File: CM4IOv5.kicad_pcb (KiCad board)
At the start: 4 copper layers, 85.1 x 55.9 mm, 120 parts, among them J1 Conn_01x02, J10 HDMI_C_1.4, J11 HDMI_C_1.4, J12 Conn_02x07_Odd_Even, J13 Conn_01x03, J14 Conn_01x03, J15 Audio OUT, J16 Micro_SD_Card_Det, J2 Bus_M.2_Socket_B, J3 USB_OTG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

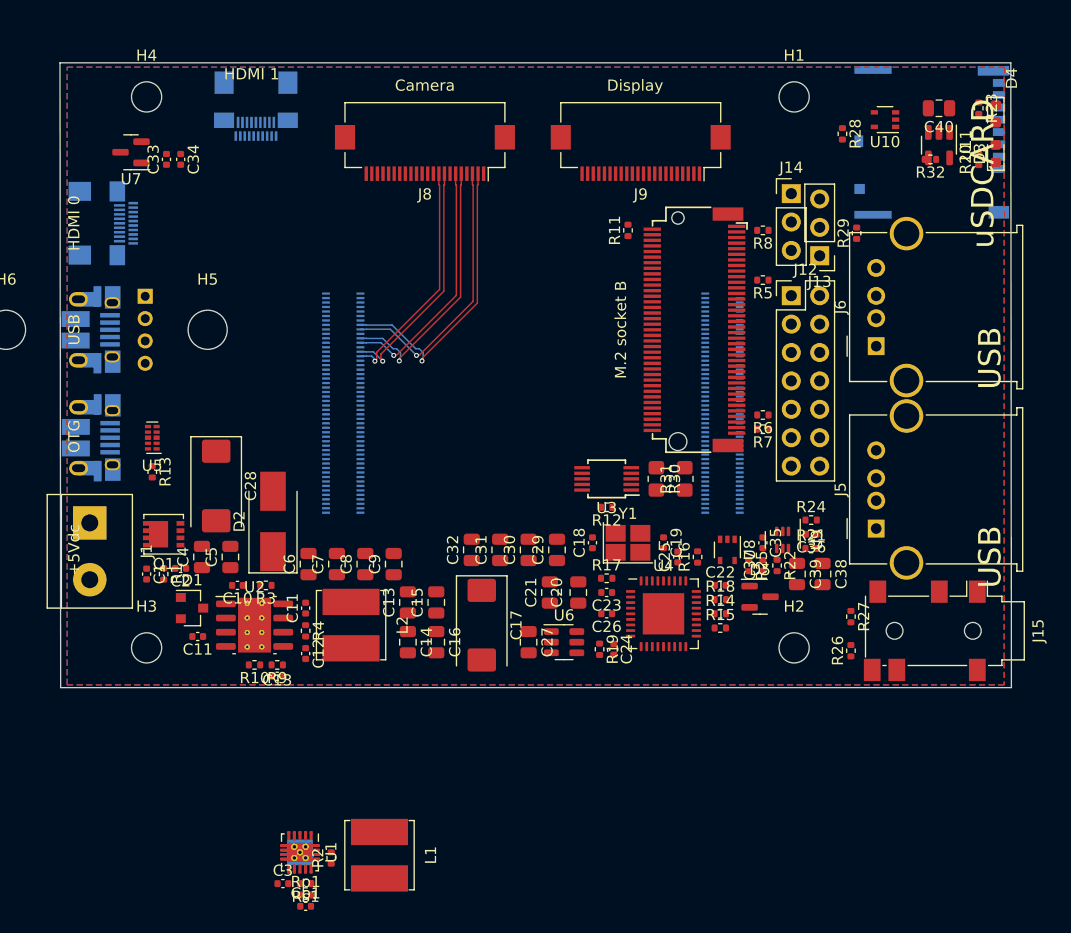
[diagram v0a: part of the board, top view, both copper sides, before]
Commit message: Initial routing of high speed signals
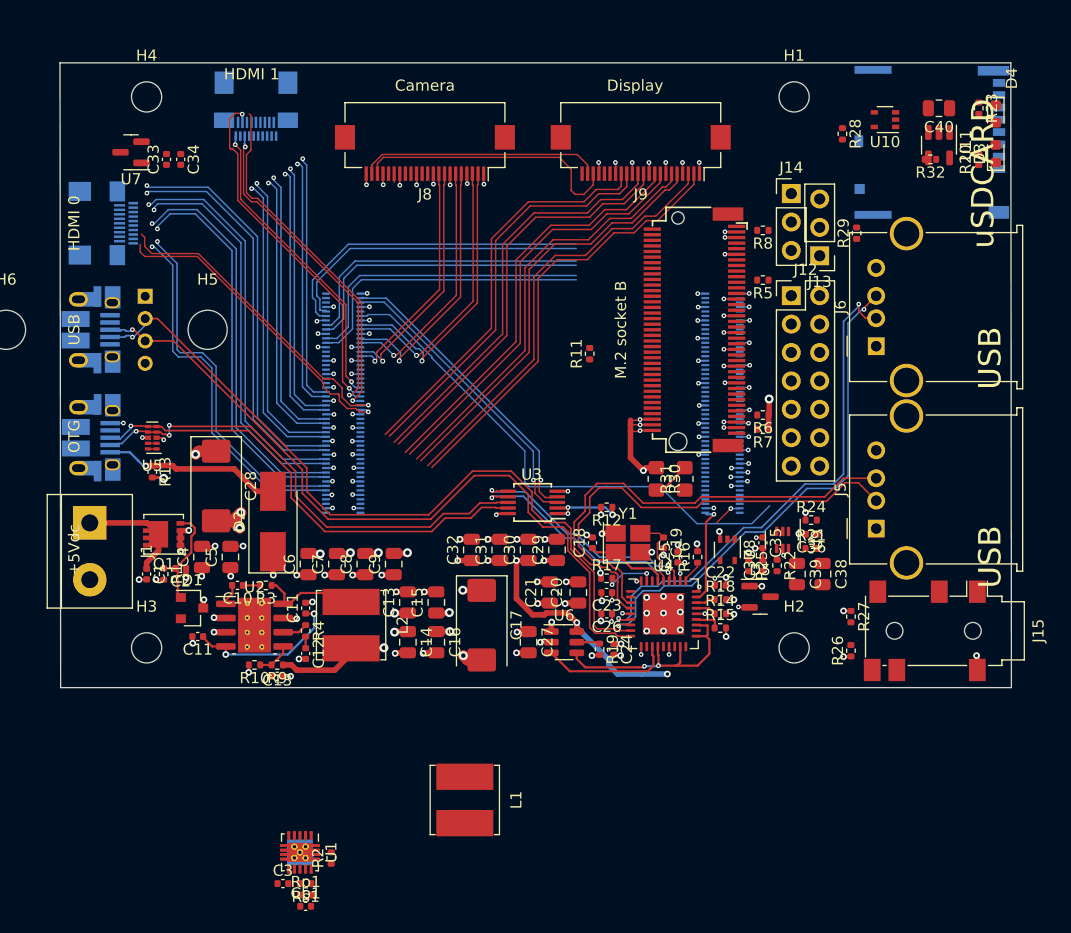
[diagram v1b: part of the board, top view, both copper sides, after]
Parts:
- moved R11 11.5 mm to (164.2, 105.0)
- moved L1 9.09 mm to (153.0, 144.9)
- moved U3 6.95 mm to (159.1, 118.3)
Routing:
- net GND: track 530.4 -> 119.2 mm, vias 0 -> 143
- net /+3.3v: track 0.00 -> 148.0 mm, vias 0 -> 27
- net /USB2-HUB/VBUS: track 0.00 -> 115.3 mm, vias 0 -> 7
- net /+5v: track 4.09 -> 116.8 mm, vias 0 -> 21
- net /USB2-HUB/HD4_N: track 0.00 -> 69.4 mm, vias 0 -> 1
- net /USB2-HUB/HD4_P: track 0.00 -> 68.3 mm, vias 0 -> 1
- net /+3.3vSSD: track 0.00 -> 68.1 mm, vias 0 -> 7
- net /CM4_GPIO (GPIO, SDCARD)/TV_OUT: track 0.00 -> 46.8 mm
- net /USB2-HUB/HD3_N: track 0.00 -> 45.9 mm, vias 0 -> 2
- net /USB2-HUB/HD3_P: track 0.00 -> 45.5 mm, vias 0 -> 2
- net /USB2-HUB/USBD_N: track 0.00 -> 43.1 mm, vias 0 -> 3
- net /USB2-HUB/USBD_P: track 0.00 -> 42.3 mm, vias 0 -> 1
- net /USB2-HUB/HD2_P: track 0.00 -> 41.8 mm
- net /USB2-HUB/HD2_N: track 0.00 -> 41.3 mm
- net /CM4_HighSpeed/DSI1_D0_N: track 0.00 -> 39.2 mm
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- removed copper zone on In2.Cu, net /+3.3v
- removed copper zone on B.Cu, net GND
- removed copper zone on F.Cu, net GND
- removed copper zone on In2.Cu, net GND

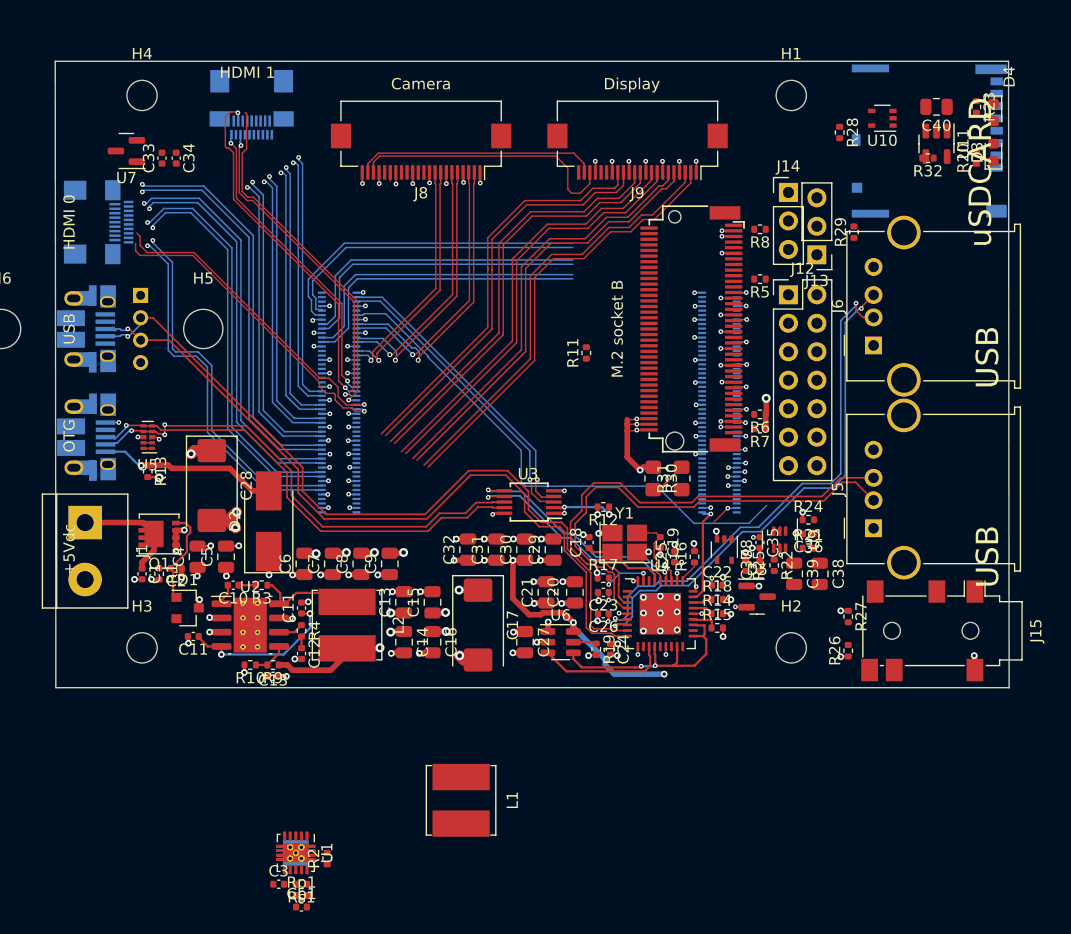
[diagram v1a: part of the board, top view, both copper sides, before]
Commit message: Aditional routing
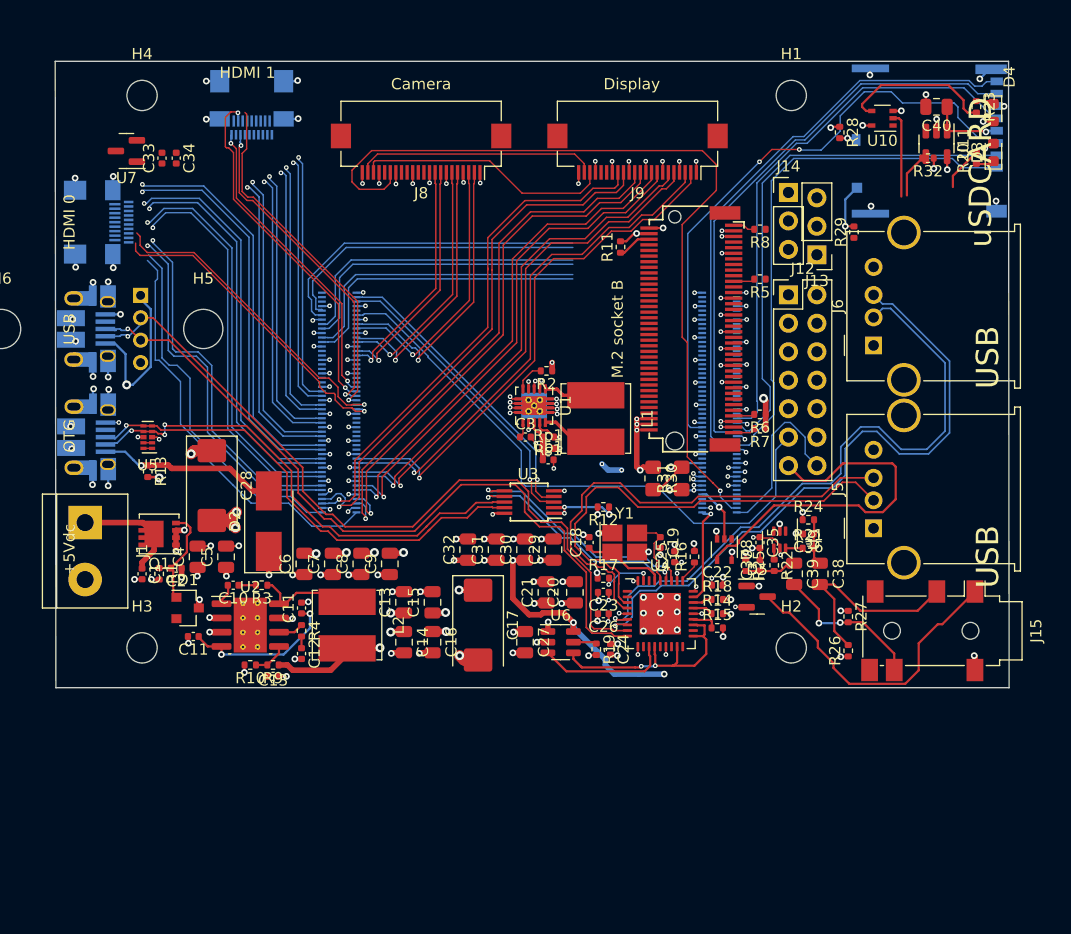
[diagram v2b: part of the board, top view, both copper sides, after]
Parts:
- moved R2 47.7 mm to (160.7, 106.6), turned to 180 degrees
- moved Cp1 45.6 mm to (160.8, 114.5)
- moved Rp1 45.6 mm to (160.8, 113.5)
- moved Rs1 45.6 mm to (160.8, 112.5)
- moved C3 45.6 mm to (158.8, 112.5)
- moved U1 45.2 mm to (159.6, 109.7)
- moved L1 36.1 mm to (165.1, 110.8)
- moved R11 9.93 mm to (167.2, 95.5)
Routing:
- net /+3.3v: track 148.0 -> 254.6 mm, vias 27 -> 37
- net /+5v: track 116.8 -> 188.3 mm, vias 21 -> 26
- net /CM4_HighSpeed/CAM_GPIO: track 3.36 -> 73.9 mm
- net /CM4_GPIO (GPIO, SDCARD)/SD_CMD: track 0.00 -> 54.5 mm, vias 0 -> 2
- net /CM4_GPIO (GPIO, SDCARD)/SD_DAT1: track 0.00 -> 53.0 mm
- net /CM4_GPIO (GPIO, SDCARD)/SD_DAT0: track 0.00 -> 51.4 mm
- net /CM4_GPIO (GPIO, SDCARD)/SD_CLK: track 0.00 -> 48.6 mm
- net /CM4_GPIO (GPIO, SDCARD)/SD_DAT2: track 0.00 -> 47.0 mm
- net /CM4_GPIO (GPIO, SDCARD)/SD_DAT3: track 0.00 -> 46.4 mm
- net GND: track 119.2 -> 160.0 mm, vias 143 -> 186
- net /CM4_HighSpeed/HDMI0_SDA: track 0.00 -> 36.8 mm
- net Net-(J12-Pad13): track 0.00 -> 32.8 mm
- net /CM4_HighSpeed/HDMI0_SCL: track 0.00 -> 32.4 mm
- net Net-(D5-Pad3): track 0.00 -> 27.1 mm
- net /USB2-HUB/VBUS: track 115.3 -> 140.3 mm, vias 7 -> 8
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
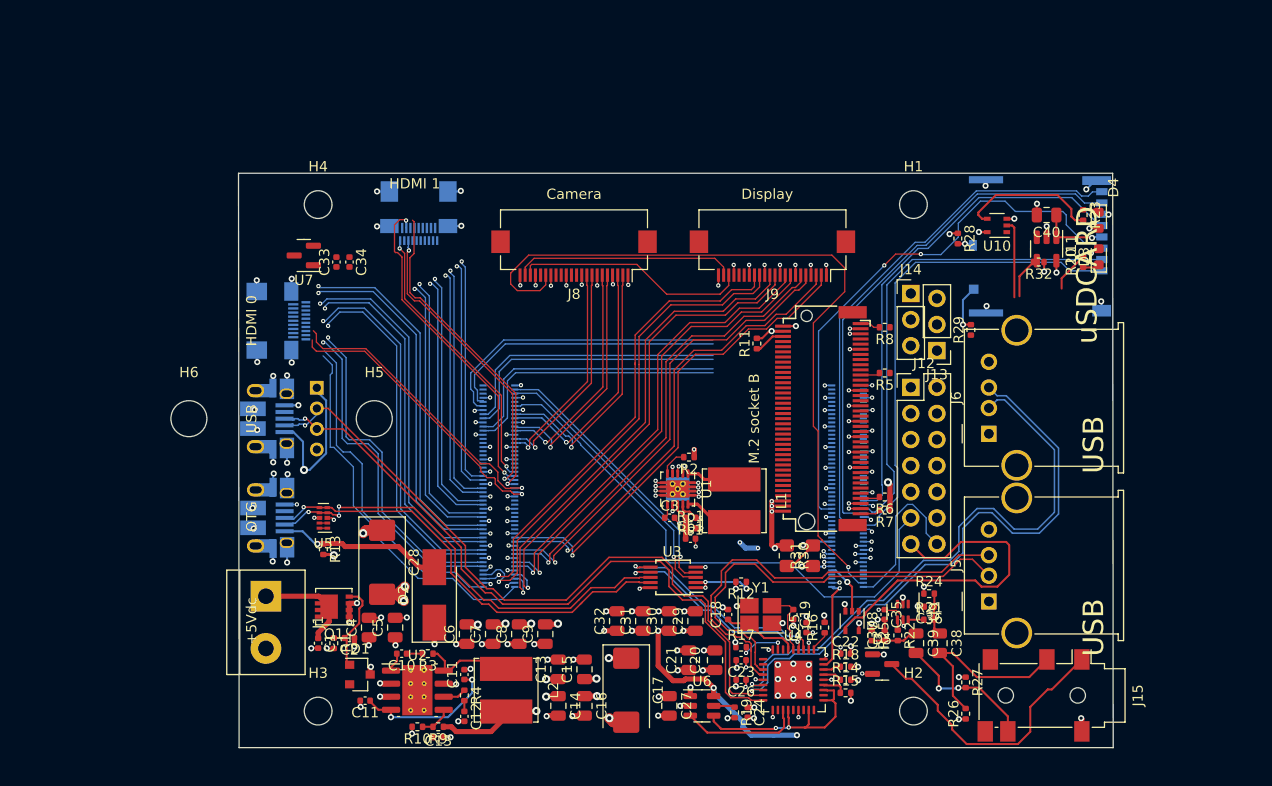
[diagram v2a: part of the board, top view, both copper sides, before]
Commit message: Adding normal size HDMI connectors
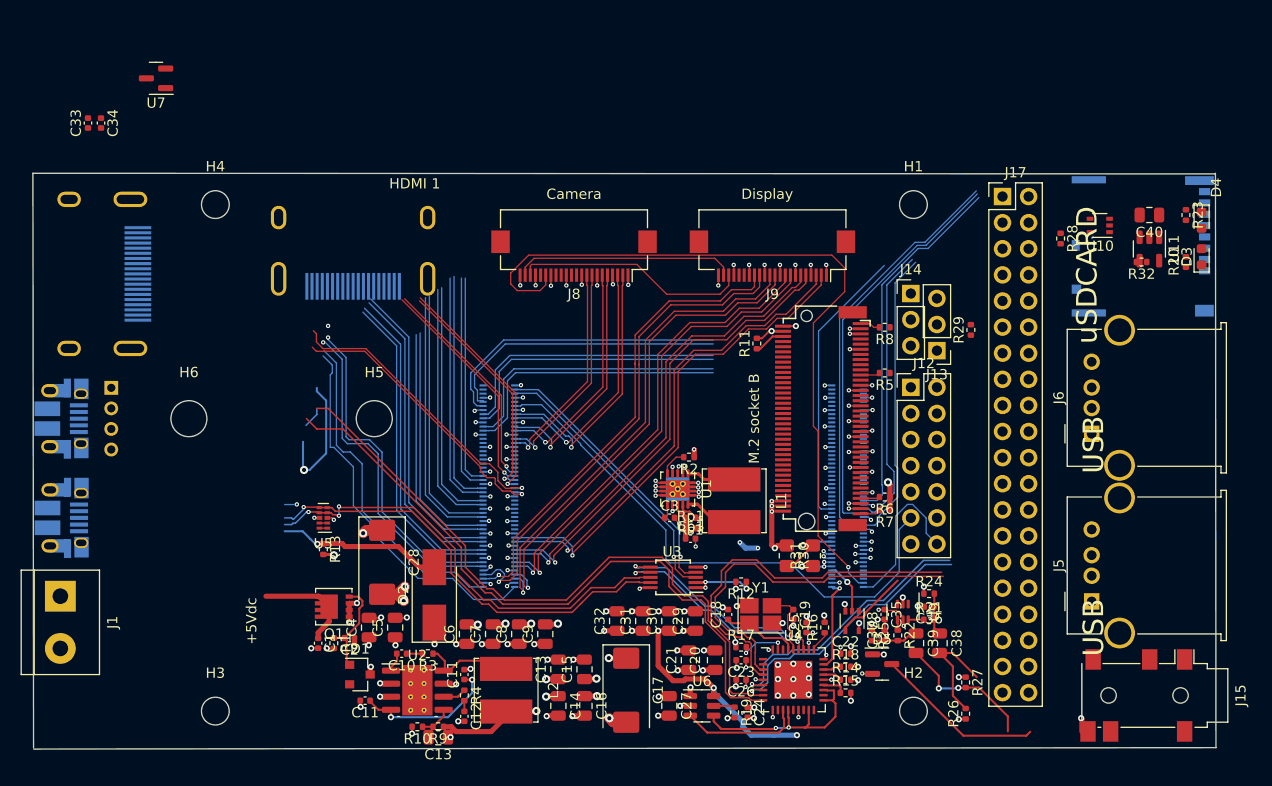
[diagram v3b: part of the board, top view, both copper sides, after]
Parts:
- added J17: THD-20-R, Connector_PinHeader_2.54mm:PinHeader_2x20_P2.54mm_Vertical, F.Cu at (191.2, 81.2)
- C11: value nf -> 100n
- C13: value nf -> 10u; footprint Capacitor_SMD:C_0402_1005Metric -> Capacitor_SMD:C_0805_2012Metric
- J10, J11: footprint Connector_HDMI:HDMI_Micro-D_Molex_46765-0x01 -> CM4IO:EDAC 690-019-298-412
- moved C34 27.7 mm to (103.5, 74.1)
- moved C33 27.7 mm to (102.2, 74.1)
- moved U7 22.4 mm to (108.8, 69.8)
- moved J1 20.0 mm to (99.5, 120.1)
- moved J3 20.0 mm to (98.5, 112.5)
- moved J4 20.0 mm to (104.4, 99.9)
- moved J7 20.0 mm to (98.5, 102.9)
- moved J10 13.1 mm to (106.3, 88.8)
- moved J11 10.6 mm to (128.0, 89.3)
- moved C40 10.0 mm to (205.4, 83.0)
- moved D3 10.0 mm to (210.5, 87.1)
- moved D4 10.0 mm to (210.5, 83.6)
- moved H3 10.0 mm to (114.6, 131.3)
- moved H4 10.0 mm to (114.6, 82.0)
- moved J15 10.0 mm to (204.2, 129.8)
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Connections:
- C13 pad 1: /+3.3v -> /+3.3vSSD
- C13 pad 2: Net-(C13-Pad2) -> GND
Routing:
- net /+3.3vSSD: track 86.6 -> 0.00 mm, vias 9 -> 0
- net /+3.3v: track 254.6 -> 318.5 mm, vias 37 -> 40
- net /USB2-HUB/HD3_P: track 57.8 -> 26.6 mm
- net /USB2-HUB/HD3_N: track 56.4 -> 26.5 mm
- net GND: track 160.0 -> 130.2 mm, vias 186 -> 157
- net /CM4_GPIO (GPIO, SDCARD)/SD_CMD: track 54.5 -> 27.5 mm, vias 2 -> 0
- net /USB2-HUB/VBUS: track 140.3 -> 113.9 mm
- net Net-(J12-Pin_13): track 32.8 -> 7.44 mm
- net /CM4_GPIO (GPIO, SDCARD)/SD_DAT2: track 47.0 -> 28.5 mm
- net /CM4_GPIO (GPIO, SDCARD)/SD_DAT3: track 46.4 -> 27.9 mm
- net Net-(R23-Pad2): track 13.6 -> 0.00 mm
- net /CM4_GPIO (GPIO, SDCARD)/SD_CLK: track 48.6 -> 35.5 mm
- net /CM4_GPIO (GPIO, SDCARD)/SD_DAT1: track 53.0 -> 40.4 mm
- net /CM4_GPIO (GPIO, SDCARD)/SD_DAT0: track 51.4 -> 38.9 mm
- net /CM4_HighSpeed/HDMI0_D2_P: track 35.1 -> 23.4 mm, vias 1 -> 0
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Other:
- board size 85.1 x 55.9 mm -> 115.1 x 56 mm
- board text removed: "HDMI 0"
- board text removed: "OTG"

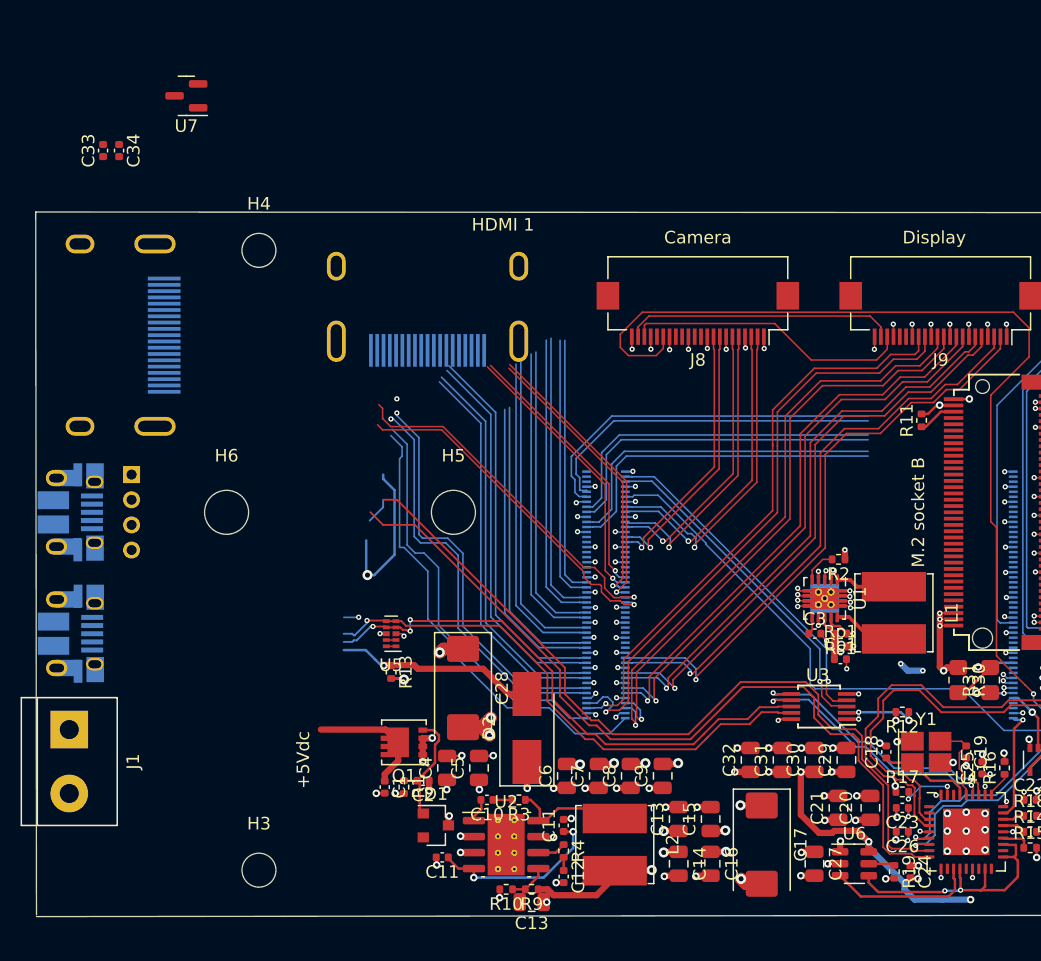
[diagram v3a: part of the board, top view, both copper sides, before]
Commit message: Adding 3D modesl
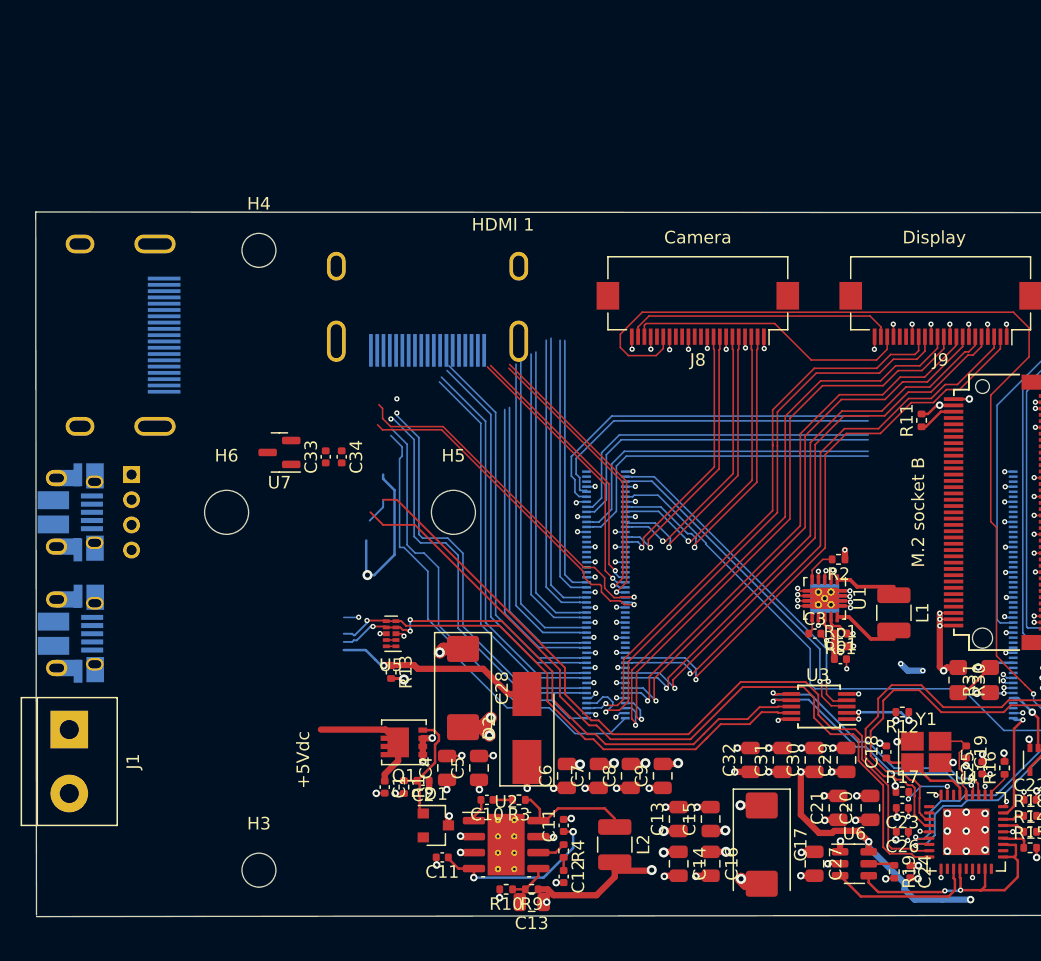
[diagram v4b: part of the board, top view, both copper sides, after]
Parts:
- L1, L2: footprint Inductor_SMD:L_Bourns_SRN6045TA -> Inductor_SMD:L_1210_3225Metric
- moved C34 30.1 mm to (121.2, 98.5)
- moved C33 30.1 mm to (119.9, 98.5)
- moved U7 29.3 mm to (116.2, 98.1)
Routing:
- net /CM4_HighSpeed/HDMI0_D1_P: track 30.0 -> 0.00 mm
- net /CM4_HighSpeed/HDMI1_D1_N: track 23.3 -> 53.3 mm
